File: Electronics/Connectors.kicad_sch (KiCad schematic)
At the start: 56 parts, among them J501 Switches, J502 Motor Con, J503 Hall Sensor, Q501 BC817, U501 ‎ACHS-7124-000E‎, U502 LM393, U503 74AHC08, U504 MCP6001-OT

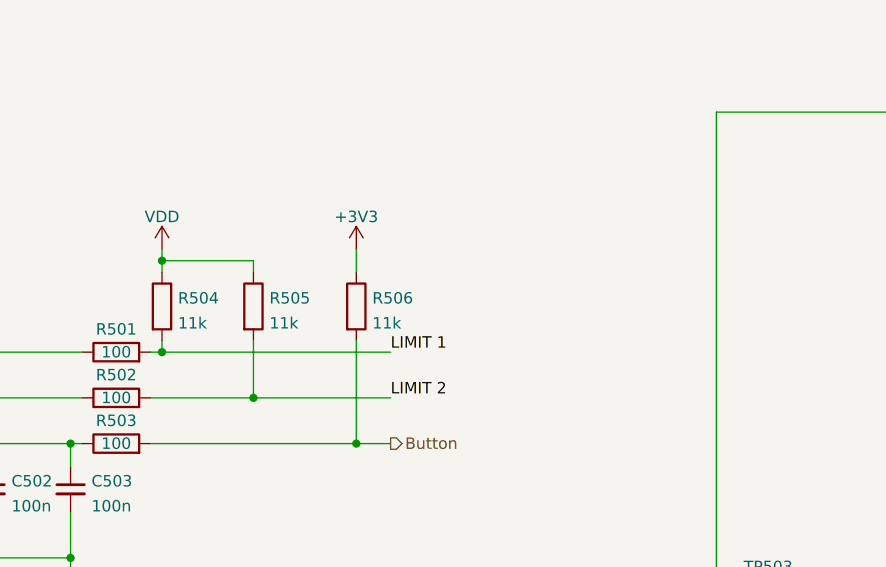
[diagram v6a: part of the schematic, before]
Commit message: Chaned 74AHC08 footprint to ssop-14
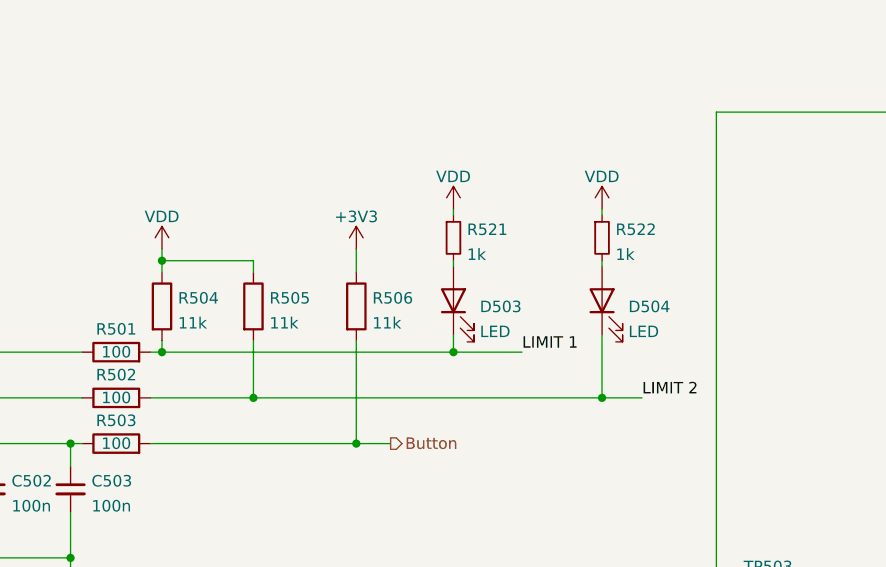
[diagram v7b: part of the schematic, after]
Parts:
- added D503, D504: LED, LED_SMD:LED_1206_3216Metric_Pad1.42x1.75mm_HandSolder, symbol Device:LED
- added R521, R522: 1k, LED_SMD:LED_0603_1608Metric_Pad1.05x0.95mm_HandSolder, symbol Device:R_Small
- U503: footprint Package_SO:SO-14_3.9x8.65mm_P1.27mm -> Package_SO:SSOP-14_5.3x6.2mm_P0.65mm
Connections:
- net LIMIT 1: now also D503.1 (K)
- net LIMIT 2: now also D504.1 (K)
- net VDD: now also R521.1, R522.1
- new net: D504.2 (A), R522.2
- new net: D503.2 (A), R521.2
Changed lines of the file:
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@@
   (junction (at 77.47 134.62) (diameter 0) (color 0 0 0 0)
   )
+  (junction (at 109.855 68.58) (diameter 0) (color 0 0 0 0)
+  )
   (junction (at 190.5 28.575) (diameter 0) (color 0 0 0 0)
   )
@@
   )
   (junction (at 139.065 114.935) (diameter 0) (color 0 0 0 0)
+  )
+  (junction (at 126.365 73.66) (diameter 0) (color 0 0 0 0)
   )
   (junction (at 241.3 158.115) (diameter 0) (color 0 0 0 0)
@@
     (stroke (width 0) (type default) (color 0 0 0 0))
   )
+  (wire (pts (xy 109.855 66.675) (xy 109.855 68.58))
+    (stroke (width 0) (type default) (color 0 0 0 0))
+  )
   (wire (pts (xy 216.535 102.235) (xy 221.615 102.235))
     (stroke (width 0) (type default) (color 0 0 0 0))
@@
     (stroke (width 0) (type default) (color 0 0 0 0))
   )
+  (wire (pts (xy 109.855 68.58) (xy 117.475 68.58))
+    (stroke (width 0) (type default) (color 0 0 0 0))
+  )
   (wire (pts (xy 77.47 113.03) (xy 87.63 113.03))
     (stroke (width 0) (type default) (color 0 0 0 0))
   )
+  (wire (pts (xy 126.365 52.705) (xy 126.365 53.34))
+    (stroke (width 0) (type default) (color 0 0 0 0))
+  )
   (wire (pts (xy 231.14 102.235) (xy 231.14 104.775))
     (stroke (width 0) (type default) (color 0 0 0 0))
@@
     (stroke (width 0) (type default) (color 0 0 0 0))
   )
-  (wire (pts (xy 87.63 73.66) (xy 102.87 73.66))
+  (wire (pts (xy 87.63 73.66) (xy 126.365 73.66))
     (stroke (width 0) (type default) (color 0 0 0 0))
   )
@@
     (stroke (width 0) (type default) (color 0 0 0 0))
   )
+  (wire (pts (xy 109.855 52.705) (xy 109.855 53.34))
+    (stroke (width 0) (type default) (color 0 0 0 0))
+  )
   (wire (pts (xy 48.26 91.44) (xy 48.26 86.36))
     (stroke (width 0) (type default) (color 0 0 0 0))
   )
+  (wire (pts (xy 126.365 66.675) (xy 126.365 73.66))
+    (stroke (width 0) (type default) (color 0 0 0 0))
+  )
   (wire (pts (xy 96.52 129.54) (xy 102.87 129.54))
     (stroke (width 0) (type default) (color 0 0 0 0))
@@
     (stroke (width 0) (type default) (color 0 0 0 0))
   )
+  (wire (pts (xy 126.365 58.42) (xy 126.365 59.055))
+    (stroke (width 0) (type default) (color 0 0 0 0))
+  )
   (wire (pts (xy 203.2 90.805) (xy 203.2 93.98))
     (stroke (width 0) (type default) (color 0 0 0 0))
@@
     (stroke (width 0) (type default) (color 0 0 0 0))
   )
+  (wire (pts (xy 126.365 73.66) (xy 130.81 73.66))
+    (stroke (width 0) (type default) (color 0 0 0 0))
+  )
   (wire (pts (xy 224.155 114.935) (xy 231.14 114.935))
     (stroke (width 0) (type default) (color 0 0 0 0))
@@
     (stroke (width 0) (type default) (color 0 0 0 0))
   )
+  (wire (pts (xy 109.855 58.42) (xy 109.855 59.055))
+    (stroke (width 0) (type default) (color 0 0 0 0))
+  )
   (wire (pts (xy 129.54 116.205) (xy 139.065 116.205))
     (stroke (width 0) (type default) (color 0 0 0 0))
@@
     (stroke (width 0) (type default) (color 0 0 0 0))
   )
-  (wire (pts (xy 77.47 68.58) (xy 102.87 68.58))
+  (wire (pts (xy 77.47 68.58) (xy 109.855 68.58))
     (stroke (width 0) (type default) (color 0 0 0 0))
   )
@@
     (effects (font (size 1.27 1.27)) (justify right bottom))
   )
-  (label "LIMIT 2" (at 102.87 73.66 0)
+  (label "LIMIT 2" (at 130.81 73.66 0)
     (effects (font (size 1.27 1.27)) (justify left bottom))
   )
-  (label "LIMIT 1" (at 102.87 68.58 0)
+  (label "LIMIT 1" (at 117.475 68.58 0)
     (effects (font (size 1.27 1.27)) (justify left bottom))
   )
@@
     (pin "2")
   )
+  (symbol (lib_id "power:VDD") (at 126.365 52.705 0) (unit 1)
+    (in_bom yes) (on_board yes) (fields_autoplaced)
+    (property "Reference" "#PWR0523" (id 0) (at 126.365 56.515 0)
+      (effects (font (size 1.27 1.27)) hide)
+    )
+    (property "Value" "VDD" (id 1) (at 126.365 49.1005 0))
+    (property "Footprint" "" (id 2) (at 126.365 52.705 0)
+      (effects (font (size 1.27 1.27)) hide)
+    )
+    (property "Datasheet" "" (id 3) (at 126.365 52.705 0)
+      (effects (font (size 1.27 1.27)) hide)
+    )
+    (pin "1")
+  )
   (symbol (lib_id "power:GND") (at 241.3 159.385 0) (unit 1)
     (in_bom yes) (on_board yes) (fields_autoplaced)
@@
       (effects (font (size 1.27 1.27)) (justify left))
     )
-    (property "Footprint" "Package_SO:SO-14_3.9x8.65mm_P1.27mm" (id 2) (at 137.16 174.625 0)
+    (property "Footprint" "Package_SO:SSOP-14_5.3x6.2mm_P0.65mm" (id 2) (at 137.16 174.625 0)
       (effects (font (size 1.27 1.27)) hide)
     )
@@
     (property "Reference" "U503" (id 0) (at 253.365 109.6985 0))
     (property "Value" "74AHC08" (id 1) (at 253.365 112.4736 0))
-    (property "Footprint" "Package_SO:SO-14_3.9x8.65mm_P1.27mm" (id 2) (at 253.365 117.475 0)
+    (property "Footprint" "Package_SO:SSOP-14_5.3x6.2mm_P0.65mm" (id 2) (at 253.365 117.475 0)
       (effects (font (size 1.27 1.27)) hide)
     )
@@
     (pin "1")
   )
+  (symbol (lib_id "Device:LED") (at 126.365 62.865 90) (unit 1)
+    (in_bom yes) (on_board yes) (fields_autoplaced)
+    (property "Reference" "D504" (id 0) (at 129.286 63.544 90)
+      (effects (font (size 1.27 1.27)) (justify right))
+    )
+    (property "Value" "LED" (id 1) (at 129.286 66.3191 90)
+      (effects (font (size 1.27 1.27)) (justify right))
+    )
+    (property "Footprint" "LED_SMD:LED_1206_3216Metric_Pad1.42x1.75mm_HandSolder" (id 2) (at 126.365 62.865 0)
+      (effects (font (size 1.27 1.27)) hide)
+    )
+    (property "Datasheet" "~" (id 3) (at 126.365 62.865 0)
+      (effects (font (size 1.27 1.27)) hide)
+    )
+    (pin "1")
+    (pin "2")
+  )
   (symbol (lib_id "dk_Tactile-Switches:B3U-1000P") (at 205.74 147.32 270) (mirror x) (unit 1)
     (in_bom yes) (on_board yes) (fields_autoplaced)
@@
     (pin "2")
   )
+  (symbol (lib_id "power:VDD") (at 109.855 52.705 0) (unit 1)
+    (in_bom yes) (on_board yes) (fields_autoplaced)
+    (property "Reference" "#PWR0503" (id 0) (at 109.855 56.515 0)
+      (effects (font (size 1.27 1.27)) hide)
+    )
+    (property "Value" "VDD" (id 1) (at 109.855 49.1005 0))
+    (property "Footprint" "" (id 2) (at 109.855 52.705 0)
+      (effects (font (size 1.27 1.27)) hide)
+    )
+    (property "Datasheet" "" (id 3) (at 109.855 52.705 0)
+      (effects (font (size 1.27 1.27)) hide)
+    )
+    (pin "1")
+  )
   (symbol (lib_id "Device:C_Small") (at 67.31 83.82 0) (unit 1)
     (in_bom yes) (on_board yes) (fields_autoplaced)
@@
     (pin "1")
   )
+  (symbol (lib_id "Device:R_Small") (at 109.855 55.88 0) (unit 1)
+    (in_bom yes) (on_board yes) (fields_autoplaced)
+    (property "Reference" "R521" (id 0) (at 111.3536 54.9715 0)
+      (effects (font (size 1.27 1.27)) (justify left))
+    )
+    (property "Value" "1k" (id 1) (at 111.3536 57.7466 0)
+      (effects (font (size 1.27 1.27)) (justify left))
+    )
+    (property "Footprint" "LED_SMD:LED_0603_1608Metric_Pad1.05x0.95mm_HandSolder" (id 2) (at 109.855 55.88 0)
+      (effects (font (size 1.27 1.27)) hide)
+    )
+    (property "Datasheet" "~" (id 3) (at 109.855 55.88 0)
+      (effects (font (size 1.27 1.27)) hide)
+    )
+    (pin "1")
+    (pin "2")
+  )
   (symbol (lib_id "power:VD") (at 220.98 40.64 0) (unit 1)
     (in_bom yes) (on_board yes) (fields_autoplaced)
@@
     (pin "1")
   )
+  (symbol (lib_id "Device:R_Small") (at 126.365 55.88 0) (unit 1)
+    (in_bom yes) (on_board yes) (fields_autoplaced)
+    (property "Reference" "R522" (id 0) (at 127.8636 54.9715 0)
+      (effects (font (size 1.27 1.27)) (justify left))
+    )
+    (property "Value" "1k" (id 1) (at 127.8636 57.7466 0)
+      (effects (font (size 1.27 1.27)) (justify left))
+    )
+    (property "Footprint" "LED_SMD:LED_0603_1608Metric_Pad1.05x0.95mm_HandSolder" (id 2) (at 126.365 55.88 0)
+      (effects (font (size 1.27 1.27)) hide)
+    )
+    (property "Datasheet" "~" (id 3) (at 126.365 55.88 0)
+      (effects (font (size 1.27 1.27)) hide)
+    )
+    (pin "1")
+    (pin "2")
+  )
   (symbol (lib_id "power:GND") (at 139.065 127 0) (unit 1)
     (in_bom yes) (on_board yes) (fields_autoplaced)
@@
     (property "Reference" "U503" (id 0) (at 252.73 147.7985 0))
     (property "Value" "74AHC08" (id 1) (at 252.73 150.5736 0))
-    (property "Footprint" "Package_SO:SO-14_3.9x8.65mm_P1.27mm" (id 2) (at 252.73 155.575 0)
+    (property "Footprint" "Package_SO:SSOP-14_5.3x6.2mm_P0.65mm" (id 2) (at 252.73 155.575 0)
       (effects (font (size 1.27 1.27)) hide)
     )
@@
     (pin "1")
   )
+  (symbol (lib_id "Device:LED") (at 109.855 62.865 90) (unit 1)
+    (in_bom yes) (on_board yes) (fields_autoplaced)
+    (property "Reference" "D503" (id 0) (at 112.776 63.544 90)
+      (effects (font (size 1.27 1.27)) (justify right))
+    )
+    (property "Value" "LED" (id 1) (at 112.776 66.3191 90)
+      (effects (font (size 1.27 1.27)) (justify right))
+    )
+    (property "Footprint" "LED_SMD:LED_1206_3216Metric_Pad1.42x1.75mm_HandSolder" (id 2) (at 109.855 62.865 0)
+      (effects (font (size 1.27 1.27)) hide)
+    )
+    (property "Datasheet" "~" (id 3) (at 109.855 62.865 0)
+      (effects (font (size 1.27 1.27)) hide)
+    )
+    (pin "1")
+    (pin "2")
+  )
   (symbol (lib_id "power:GND") (at 205.74 156.21 0) (unit 1)
     (in_bom yes) (on_board yes) (fields_autoplaced)
@@
     (property "Reference" "U503" (id 0) (at 229.87 147.7985 0))
     (property "Value" "74AHC08" (id 1) (at 229.87 150.5736 0))
-    (property "Footprint" "Package_SO:SO-14_3.9x8.65mm_P1.27mm" (id 2) (at 229.87 155.575 0)
+    (property "Footprint" "Package_SO:SSOP-14_5.3x6.2mm_P0.65mm" (id 2) (at 229.87 155.575 0)
       (effects (font (size 1.27 1.27)) hide)
     )
@@
     (property "Reference" "U503" (id 0) (at 253.365 123.0335 0))
     (property "Value" "74AHC08" (id 1) (at 253.365 125.8086 0))
-    (property "Footprint" "Package_SO:SO-14_3.9x8.65mm_P1.27mm" (id 2) (at 253.365 130.81 0)
-      (effects (font (size 1.27 1.27)) hide)
-    )
+    (property "Footprint" "Package_SO:SSOP-14_5.3x6.2mm_P0.65mm" (id 2) (at 253.365 130.81 0)
+      (effects (font (size 1.27 1.27)) hide)
+    )

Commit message: Layout improvements
Signed-off-by: Aki Kuusela <git@findersee.fi>
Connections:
- net +3V3: now also U503.13
- net GND: no longer U503.12, U503.13
- net at D501.1 (K), D502.1 (K), R517.2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: now also U503.12
- net Over Current: now reaches U503.11
- net LIMIT 1 renamed Limit_1
- net LIMIT 2 renamed Limit_2
- no-connect marks 1 -> 3
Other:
- company: (none) -> findersee.fi
- title: (none) -> Motor Controller
- moved on the sheet: U503C, U503D
